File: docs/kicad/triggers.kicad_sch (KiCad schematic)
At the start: 2 parts, among them SW2 Rev Trigger, SW3 Firing Trigger

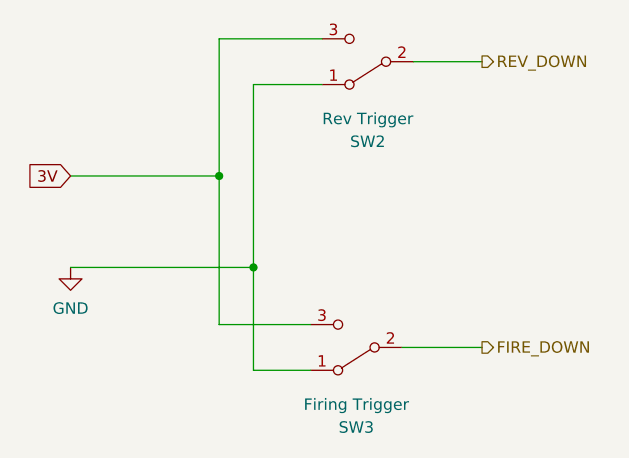
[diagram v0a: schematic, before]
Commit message: Updating PCB to match schematic.
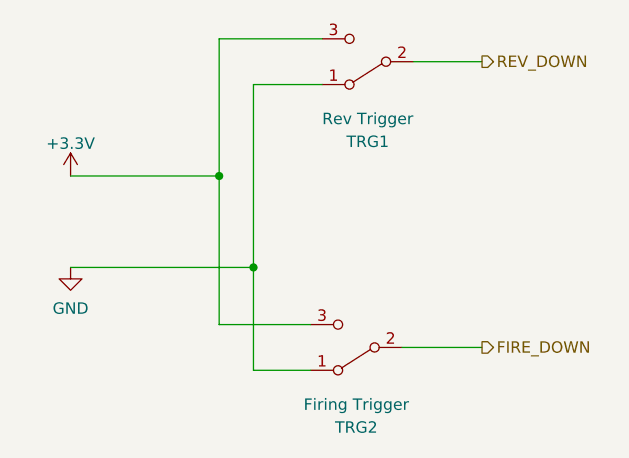
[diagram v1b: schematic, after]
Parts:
- renumbered SW2 to TRG1, SW3 to TRG2
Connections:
- net 3V renamed +3V3
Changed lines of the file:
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@@
     (stroke (width 0) (type default) (color 0 0 0 0))
-  )
-  (global_label "3V" (shape input) (at 106.68 90.17 180) (fields_autoplaced)
-    (effects (font (size 1.27 1.27)) (justify right))
-    (property "Intersheet References" "${INTERSHEET_REFS}" (id 0) (at 153.67 198.12 0)
-      (effects (font (size 1.27 1.27)) hide)
-    )
   )
   (hierarchical_label "REV_DOWN" (shape output) (at 152.4 77.47 0)
@@
   (hierarchical_label "FIRE_DOWN" (shape output) (at 152.4 109.22 0)
     (effects (font (size 1.27 1.27)) (justify left))
+  )
+  (symbol (lib_id "power:+3.3V") (at 106.68 90.17 0) (unit 1)
+    (in_bom yes) (on_board yes) (fields_autoplaced)
+    (property "Reference" "#PWR0119" (id 0) (at 106.68 93.98 0)
+      (effects (font (size 1.27 1.27)) hide)
+    )
+    (property "Value" "+3.3V" (id 1) (at 106.68 86.5655 0))
+    (property "Footprint" "" (id 2) (at 106.68 90.17 0)
+      (effects (font (size 1.27 1.27)) hide)
+    )
+    (property "Datasheet" "" (id 3) (at 106.68 90.17 0)
+      (effects (font (size 1.27 1.27)) hide)
+    )
+    (pin "1")
   )
   (symbol (lib_id "power:GND") (at 106.68 100.33 0) (unit 1)
@@
   (symbol (lib_id "Switch:SW_SPDT") (at 139.7 77.47 180) (unit 1)
     (in_bom yes) (on_board yes)
-    (property "Reference" "SW2" (id 0) (at 139.7 86.36 0))
+    (property "Reference" "TRG1" (id 0) (at 139.7 86.36 0))
     (property "Value" "Rev Trigger" (id 1) (at 139.7 83.82 0))
     (property "Footprint" "" (id 2) (at 139.7 77.47 0)
@@
   (symbol (lib_id "Switch:SW_SPDT") (at 138.43 109.22 180) (unit 1)
     (in_bom yes) (on_board yes)
-    (property "Reference" "SW3" (id 0) (at 138.43 118.11 0))
+    (property "Reference" "TRG2" (id 0) (at 138.43 118.11 0))
     (property "Value" "Firing Trigger" (id 1) (at 138.43 115.57 0))
     (property "Footprint" "" (id 2) (at 138.43 109.22 0)
